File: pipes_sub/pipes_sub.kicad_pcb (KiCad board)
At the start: 4 copper layers, 70.8 x 110 mm, 272 parts, among them J1 2x8 Header, J2 2x5 Header, J4 2x5 Header, U1 CD4046, U10 CD4046, U11 CD4046, U12 CD4046, U13 CD4017, U14 CD4017, U15 CD4017, U16 CD4046, U17 CD4046, U18 CD4017, U19 CD4017, U2 TL072CP, U20 GLV5549, U21 GLV5549, U22 GLV5549, U23 TL072CP, U24 TL072CP, U25 TL072CP, U26 GLV5549, U27 GLV5549, U28 GLV5549, U29 TL072CP, U3 CD4017, U30 TL072CP, U31 TL072CP, U32 GLV5549, U33 GLV5549, U34 TL072CP, U35 TL072CP, U38 TL072CP, U39 TL072CP, U4 CD4046, U5 CD4046, U6 TL072CP, U7 CD4017, U8 CD4017, U9 TL072CP

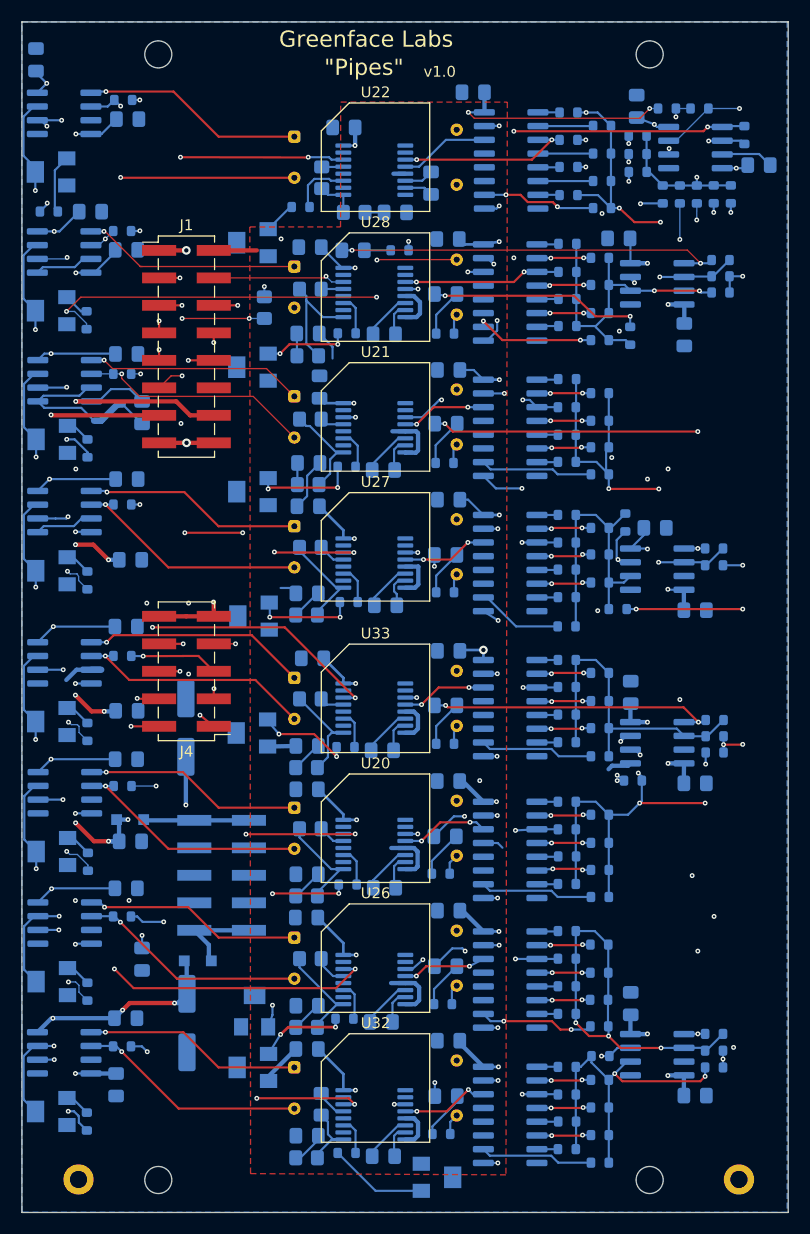
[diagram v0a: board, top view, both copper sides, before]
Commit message: Adds digikey bom merge. Uses local graphics for panel.
Adds bambooh graphics
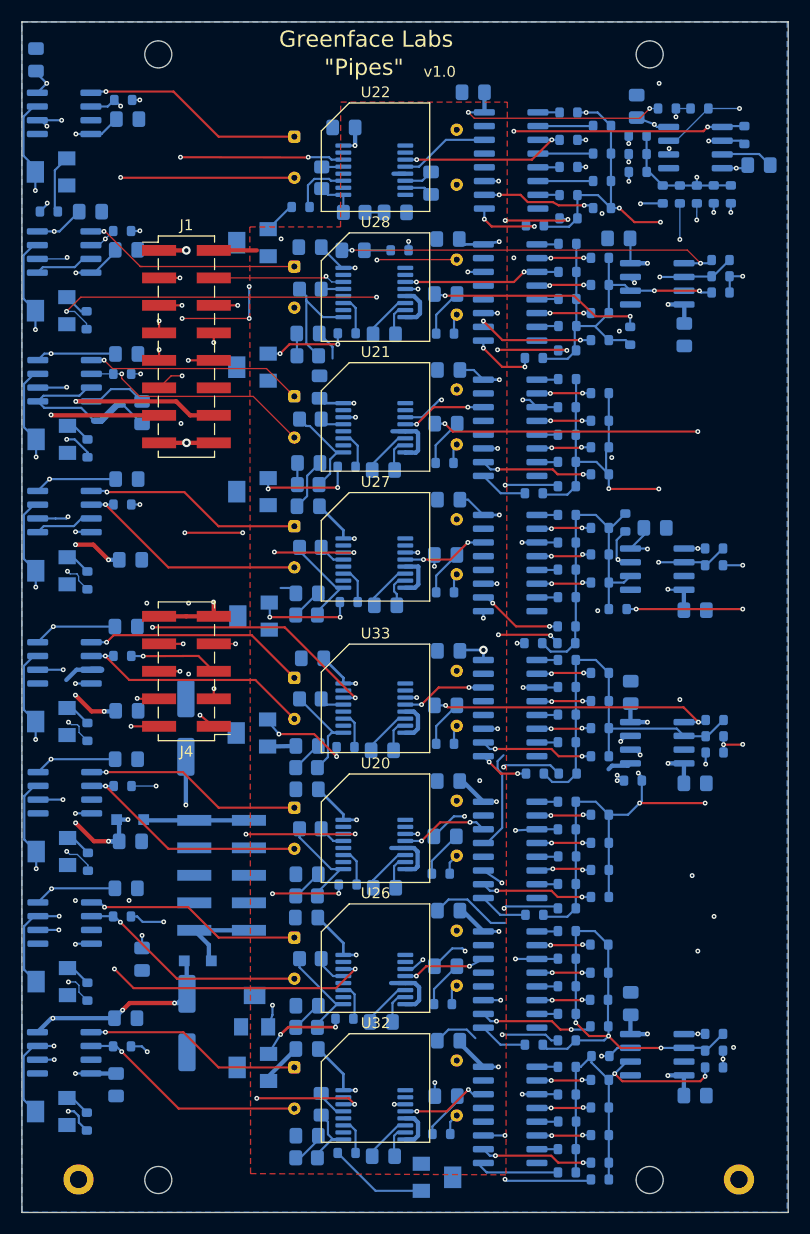
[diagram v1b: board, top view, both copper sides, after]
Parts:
- removed R2: 470, Resistor_SMD:R_0805_2012Metric_Pad1.20x1.40mm_HandSolder
- added R141: 300K, Resistor_SMD:R_0603_1608Metric, B.Cu at (87.4, 58.8)
- added R142: 300K, Resistor_SMD:R_0603_1608Metric, B.Cu at (87.3, 83.5)
- added R143: 249K, Resistor_SMD:R_0603_1608Metric, B.Cu at (90.5, 58.1)
- added R144: 249K, Resistor_SMD:R_0603_1608Metric, B.Cu at (90.3, 82.9)
- added R145: 300K, Resistor_SMD:R_0603_1608Metric, B.Cu at (87.3, 71.0)
- added R146: 300K, Resistor_SMD:R_0603_1608Metric, B.Cu at (87.2, 97.4)
- added R147: 249K, Resistor_SMD:R_0603_1608Metric, B.Cu at (90.4, 70.3)
- added R148: 249K, Resistor_SMD:R_0603_1608Metric, B.Cu at (90.3, 97.4)
- added R149: 300K, Resistor_SMD:R_0603_1608Metric, B.Cu at (87.4, 109.5)
- added R150: 300K, Resistor_SMD:R_0603_1608Metric, B.Cu at (87.3, 134.5)
- added R151: 249K, Resistor_SMD:R_0603_1608Metric, B.Cu at (90.4, 109.5)
- added R152: 249K, Resistor_SMD:R_0603_1608Metric, B.Cu at (90.3, 134.1)
- added R153: 300K, Resistor_SMD:R_0603_1608Metric, B.Cu at (90.3, 146.3)
- added R154: 300K, Resistor_SMD:R_0603_1608Metric, B.Cu at (87.3, 122.5)
- added R155: 249K, Resistor_SMD:R_0603_1608Metric, B.Cu at (93.4, 146.9)
- added R156: 249K, Resistor_SMD:R_0603_1608Metric, B.Cu at (90.3, 121.9)
- C1, C15, C21: value 4.7nF -> 300p
- C14, C22, C27, C28: value 1nF -> 300p
- C17, C18, C2, C23, C24, C25, C37, C38: value 1uF -> 10uF
- C20: value 2.2nF -> 300p
- R1, R10, R11, R12, R13, R139, R14, R140, R15, R16, R17: value 1K -> 10K
- R100, R104, R120, R124, R19, R7, R80, R84: value 300K -> 150K
- R101, R105, R121, R125, R22, R8, R81, R85: value 200K -> 165K
- R102, R106, R122, R126, R27, R82, R86, R9: value 150K -> 249K
- R107, R112, R127, R132, R28, R72, R87, R92: value 274K -> 165K
- R108, R113, R128, R133, R68, R73, R88, R93: value 274K -> 150K
- R109, R114, R129, R134, R69, R74, R89, R94: value 158K -> 200K
- R110, R115, R130, R135, R70, R75, R90, R95: value 158K -> 300K
- R20, R21, R29, R3, R30, R31, R38, R39: value 24.9K -> 10K
- R23, R25, R32, R34, R36, R4, R40, R42: value 200K -> 27K
- R24, R26, R33, R35, R37, R41, R43, R5: value 10K -> 1.5K
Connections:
- net VCO1 renamed SIG1
- net VCO2 renamed SIG2
- net VCO3 renamed SIG3
- net VCO4 renamed SIG4
- net VCO5 renamed SIG5
- net VCO6 renamed SIG6
- net VCO7 renamed SIG7
- net VCO8 renamed SIG8
- J1 pad 11: VCO -> SIG
- R1 pad 1: Net-(R1-Pad1) -> SIG
- U13 pad 11: unconnected-(U13-Pad11) -> Net-(R148-Pad1)
- U13 pad 15: Net-(U13-Pad15) -> GND
- U13 pad 9: Net-(U13-Pad15) -> Net-(R146-Pad1)
- U14 pad 11: unconnected-(U14-Pad11) -> Net-(R152-Pad1)
- U14 pad 15: Net-(U14-Pad15) -> GND
- U14 pad 9: Net-(U14-Pad15) -> Net-(R150-Pad1)
- U15 pad 11: unconnected-(U15-Pad11) -> Net-(R147-Pad1)
- U15 pad 15: Net-(U15-Pad15) -> GND
- U15 pad 9: Net-(U15-Pad15) -> Net-(R145-Pad1)
- U18 pad 11: unconnected-(U18-Pad11) -> Net-(R155-Pad1)
- U18 pad 15: Net-(U18-Pad15) -> GND
- U18 pad 9: Net-(U18-Pad15) -> Net-(R153-Pad1)
- U19 pad 11: unconnected-(U19-Pad11) -> Net-(R151-Pad1)
- U19 pad 15: Net-(U19-Pad15) -> GND
- U19 pad 9: Net-(U19-Pad15) -> Net-(R149-Pad1)
- U2 pad 1: Net-(R1-Pad1) -> SIG
- U3 pad 11: unconnected-(U3-Pad11) -> Net-(R143-Pad1)
- U3 pad 15: Net-(U3-Pad15) -> GND
- U3 pad 9: Net-(U3-Pad15) -> Net-(R141-Pad1)
- U7 pad 11: unconnected-(U7-Pad11) -> Net-(R156-Pad1)
- U7 pad 15: Net-(U7-Pad15) -> GND
- U7 pad 9: Net-(U7-Pad15) -> Net-(R154-Pad1)
- U8 pad 11: unconnected-(U8-Pad11) -> Net-(R144-Pad1)
- U8 pad 15: Net-(U8-Pad15) -> GND
- U8 pad 9: Net-(U8-Pad15) -> Net-(R142-Pad1)
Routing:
- net SIG: track 0.00 -> 75.8 mm, vias 0 -> 7
- net Net-(R1-Pad1): track 58.3 -> 0.00 mm, vias 4 -> 0
- net GND: track 103.7 -> 123.1 mm
- net VCO: track 15.5 -> 0.00 mm, vias 3 -> 0
- net Net-(U8-Pad15): track 15.4 -> 0.00 mm, vias 2 -> 0
- net Net-(R155-Pad1): track 0.00 -> 14.1 mm, vias 0 -> 2
- net Net-(R147-Pad1): track 0.00 -> 11.9 mm, vias 0 -> 3
- net Net-(R148-Pad1): track 0.00 -> 11.8 mm, vias 0 -> 3
- net Net-(R143-Pad1): track 0.00 -> 11.8 mm, vias 0 -> 3
- net Net-(U13-Pad15): track 11.4 -> 0.00 mm, vias 2 -> 0
- net Net-(R151-Pad1): track 0.00 -> 10.6 mm, vias 0 -> 2
- net Net-(U14-Pad15): track 10.5 -> 0.00 mm, vias 2 -> 0
- net Net-(U18-Pad15): track 10.3 -> 0.00 mm, vias 2 -> 0
- net Net-(U3-Pad15): track 10.3 -> 0.00 mm, vias 2 -> 0
- net Net-(U7-Pad15): track 10.2 -> 0.00 mm, vias 2 -> 0
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
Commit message: Version 1.1 of boards
Changes to use NSL-32SR3 Vactrols
Fixes 3904 package
Adds 10-step waveform
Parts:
- added C3: 30p, Capacitor_SMD:C_0805_2012Metric_Pad1.18x1.45mm_HandSolder, B.Cu at (104.5, 60.2)
- added C70: 30p, Capacitor_SMD:C_0805_2012Metric_Pad1.18x1.45mm_HandSolder, B.Cu at (103.9, 86.8)
- added C71: 30p, Capacitor_SMD:C_0805_2012Metric_Pad1.18x1.45mm_HandSolder, B.Cu at (98.2, 69.1)
- added C72: 30p, Capacitor_SMD:C_0805_2012Metric_Pad1.18x1.45mm_HandSolder, B.Cu at (98.5, 84.7)
- added C73: 30p, Capacitor_SMD:C_0805_2012Metric_Pad1.18x1.45mm_HandSolder, B.Cu at (104.0, 102.7)
- added C74: 30p, Capacitor_SMD:C_0805_2012Metric_Pad1.18x1.45mm_HandSolder, B.Cu at (103.9, 131.6)
- added C75: 30p, Capacitor_SMD:C_0805_2012Metric_Pad1.18x1.45mm_HandSolder, B.Cu at (97.2, 139.3)
- added C76: 30p, Capacitor_SMD:C_0805_2012Metric_Pad1.18x1.45mm_HandSolder, B.Cu at (93.7, 110.5)
- added R157: 200K, Resistor_SMD:R_0603_1608Metric, B.Cu at (58.3, 50.8)
- added R158: 200K, Resistor_SMD:R_0603_1608Metric, B.Cu at (52.4, 110.3)
- added R159: 200K, Resistor_SMD:R_0603_1608Metric, B.Cu at (48.7, 78.2)
- added R160: 200K, Resistor_SMD:R_0603_1608Metric, B.Cu at (49.5, 112.0)
- added R161: 200K, Resistor_SMD:R_0603_1608Metric, B.Cu at (51.1, 78.8)
- added R162: 200K, Resistor_SMD:R_0603_1608Metric, B.Cu at (49.2, 124.7)
- added R163: 200K, Resistor_SMD:R_0603_1608Metric, B.Cu at (50.6, 92.9)
- added R164: 200K, Resistor_SMD:R_0603_1608Metric, B.Cu at (50.1, 66.5)
- added R165: 200K, Resistor_SMD:R_0603_1608Metric, B.Cu at (52.5, 64.9)
- added R166: 200K, Resistor_SMD:R_0603_1608Metric, B.Cu at (50.1, 127.1)
- added R167: 200K, Resistor_SMD:R_0603_1608Metric, B.Cu at (52.4, 86.3)
- added R168: 200K, Resistor_SMD:R_0603_1608Metric, B.Cu at (49.2, 136.2)
- added R169: 200K, Resistor_SMD:R_0603_1608Metric, B.Cu at (56.9, 98.7)
- added R170: 200K, Resistor_SMD:R_0603_1608Metric, B.Cu at (49.9, 138.6)
- added R171: 200K, Resistor_SMD:R_0603_1608Metric, B.Cu at (52.9, 98.7)
- added R2: 200K, Resistor_SMD:R_0603_1608Metric, B.Cu at (55.9, 51.6)
- R100, R104, R120, R124, R19, R7, R80, R84: value 150K -> 154K
- R101, R105, R121, R125, R22, R8, R81, R85: value 165K -> 210K
- R102, R106, R122, R126, R27, R82, R86, R9: value 249K -> 300K
- R103, R119, R123, R18, R6, R79, R83, R99: value 200K -> 162K
- R107, R112, R127, R132, R28, R72, R87, R92: value 165K -> 150K
- R108, R113, R128, R133, R68, R73, R88, R93: value 150K -> 174K
- R109, R114, R129, R134, R69, R74, R89, R94: value 200K -> 261K
- R110, R115, R130, R135, R70, R75, R90, R95: value 300K -> 287K
- R141, R142, R145, R146, R149, R150, R153, R154: value 300K -> 237K
- R143, R144, R147, R148, R151, R152, R155, R156: value 249K -> 191K
- R45, R47, R49, R54, R56, R58, R63, R65: value 33K -> 220K
- R50, R51, R52, R59, R60, R61, R66, R67: value 24.9K -> 20K
- RV2, RV3, RV4, RV5, RV6, RV7, RV8, RV9: footprint sputterizer:Potentiometer_Bourns_3224W_Vertical -> Potentiometer_SMD:Potentiometer_Bourns_3224W_Vertical
- U20, U21, U22, U26, U27, U28, U32, U33: value GLV5549 -> NSL-32SR3
- moved C67 3.87 mm to (47.2, 127.0), turned to 180 degrees
- moved C57 2.09 mm to (49.6, 63.1)
- moved C69 1.74 mm to (47.1, 139.0), turned to 180 degrees
- moved C55 1.38 mm to (49.6, 50.4)
- moved R58 1.28 mm to (49.1, 60.6)
- moved R49 0.78 mm to (49.8, 47.9)
- moved R45 0.15 mm to (49.3, 110.5)
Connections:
- R45 pad 2: VCA6 -> GND
- R47 pad 2: VCA3 -> GND
- R49 pad 2: VCA1 -> GND
- R54 pad 2: VCA7 -> GND
- R56 pad 2: VCA4 -> GND
- R58 pad 2: VCA2 -> GND
- R63 pad 2: VCA8 -> GND
- R65 pad 2: VCA5 -> GND
- U20 pad 1: Net-(U20-Pad1) -> Net-(R45-Pad1)
- U20 pad 2: Net-(R45-Pad1) -> Net-(U20-Pad2)
- U21 pad 1: Net-(U21-Pad1) -> Net-(R47-Pad1)
- U21 pad 2: Net-(R47-Pad1) -> Net-(U21-Pad2)
- U22 pad 1: Net-(U22-Pad1) -> Net-(R49-Pad1)
- U22 pad 2: Net-(R49-Pad1) -> Net-(U22-Pad2)
- U23 pad 1: Net-(U20-Pad1) -> Net-(U20-Pad2)
- U23 pad 3: GND -> Net-(R158-Pad2)
- U24 pad 1: Net-(U21-Pad1) -> Net-(U21-Pad2)
- U24 pad 3: GND -> Net-(R159-Pad2)
- U25 pad 1: Net-(U22-Pad1) -> Net-(U22-Pad2)
- U25 pad 3: GND -> Net-(R157-Pad2)
- U26 pad 1: Net-(U26-Pad1) -> Net-(R54-Pad1)
- U26 pad 2: Net-(R54-Pad1) -> Net-(U26-Pad2)
- U27 pad 1: Net-(U27-Pad1) -> Net-(R56-Pad1)
- U27 pad 2: Net-(R56-Pad1) -> Net-(U27-Pad2)
- U28 pad 1: Net-(U28-Pad1) -> Net-(R58-Pad1)
- U28 pad 2: Net-(R58-Pad1) -> Net-(U28-Pad2)
- U29 pad 1: Net-(U26-Pad1) -> Net-(U26-Pad2)
- U29 pad 3: GND -> Net-(R162-Pad2)
- U30 pad 1: Net-(U27-Pad1) -> Net-(U27-Pad2)
- U30 pad 3: GND -> Net-(R163-Pad2)
- U31 pad 1: Net-(U28-Pad1) -> Net-(U28-Pad2)
- U31 pad 3: GND -> Net-(R164-Pad2)
- U32 pad 1: Net-(U32-Pad1) -> Net-(R63-Pad1)
- U32 pad 2: Net-(R63-Pad1) -> Net-(U32-Pad2)
- U33 pad 1: Net-(U33-Pad1) -> Net-(R65-Pad1)
- U33 pad 2: Net-(R65-Pad1) -> Net-(U33-Pad2)
- U34 pad 1: Net-(U32-Pad1) -> Net-(U32-Pad2)
- U34 pad 3: GND -> Net-(R168-Pad2)
- U35 pad 1: Net-(U33-Pad1) -> Net-(U33-Pad2)
- U35 pad 3: GND -> Net-(R169-Pad2)
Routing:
- net Net-(U28-Pad2): track 0.00 -> 27.9 mm, vias 0 -> 2
- net Net-(U22-Pad2): track 0.00 -> 26.6 mm, vias 0 -> 2
- net Net-(U33-Pad2): track 0.00 -> 26.2 mm, vias 0 -> 2
- net Net-(U32-Pad2): track 0.00 -> 25.9 mm, vias 0 -> 3
- net Net-(U27-Pad2): track 0.00 -> 25.8 mm, vias 0 -> 3
- net Net-(U20-Pad2): track 0.00 -> 25.1 mm, vias 0 -> 2
- net Net-(U21-Pad2): track 0.00 -> 24.9 mm, vias 0 -> 2
- net Net-(U26-Pad2): track 0.00 -> 24.8 mm, vias 0 -> 2
- net GND: track 123.1 -> 99.7 mm
- net Net-(U33-Pad1): track 20.7 -> 0.00 mm, vias 1 -> 0
- net Net-(U22-Pad1): track 20.6 -> 0.00 mm, vias 1 -> 0
- net Net-(U28-Pad1): track 20.3 -> 0.00 mm, vias 1 -> 0
- net Net-(U21-Pad1): track 20.1 -> 0.00 mm, vias 1 -> 0
- net Net-(U32-Pad1): track 20.1 -> 0.00 mm, vias 1 -> 0
- net Net-(U27-Pad1): track 20.1 -> 0.00 mm, vias 1 -> 0
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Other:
- board text added: "S/N 1.1."
- board text added: "v1.1"
- board text removed: "S/N 1.0."
- board text removed: "v1.0"

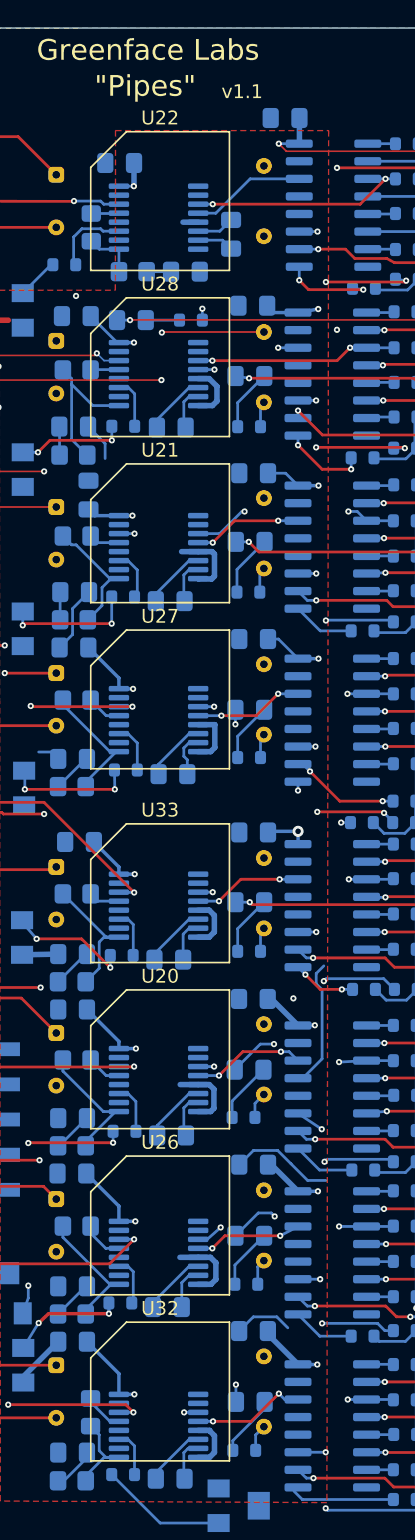
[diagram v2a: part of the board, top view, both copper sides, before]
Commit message: Uses new vactrols.
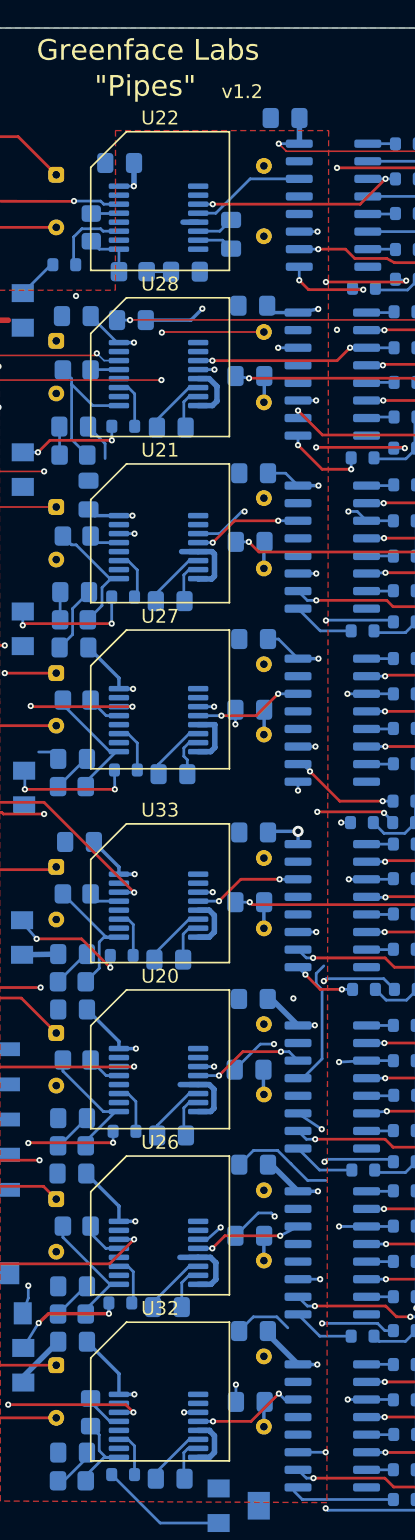
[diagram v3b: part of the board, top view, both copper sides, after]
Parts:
- removed R44, R46, R48, R53, R55, R57, R62, R64: 10K, Resistor_SMD:R_0603_1608Metric
- C46, C47, C48, C49, C50, C51, C52, C53: value 10uF -> 22uF
- R45, R47, R49, R54, R56, R58, R63, R65: value 220K -> 20K
- R50, R51, R52, R59, R60, R61, R66, R67: value 20K -> 430
- RV2, RV3, RV4, RV5, RV6, RV7, RV8, RV9: value 20K -> 500
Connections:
- C46 pad 2: Net-(C46-Pad2) -> Net-(U20-Pad4)
- C47 pad 2: Net-(C47-Pad2) -> Net-(U21-Pad4)
- C48 pad 2: Net-(C48-Pad2) -> Net-(U22-Pad4)
- C51 pad 2: Net-(C51-Pad2) -> Net-(U28-Pad4)
- C52 pad 2: Net-(C52-Pad2) -> Net-(U32-Pad4)
- U20 pad 4: Net-(R44-Pad2) -> Net-(U20-Pad4)
- U21 pad 4: Net-(R46-Pad2) -> Net-(U21-Pad4)
- U22 pad 4: Net-(R48-Pad2) -> Net-(U22-Pad4)
- U26 pad 4: Net-(R53-Pad2) -> Net-(C49-Pad2)
- U27 pad 4: Net-(R55-Pad2) -> Net-(C50-Pad2)
- U28 pad 4: Net-(R57-Pad2) -> Net-(U28-Pad4)
- U32 pad 4: Net-(R62-Pad2) -> Net-(U32-Pad4)
- U33 pad 4: Net-(R64-Pad2) -> Net-(C53-Pad2)
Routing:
- net Net-(U22-Pad4): track 0.00 -> 11.5 mm, vias 0 -> 1
- net Net-(R48-Pad2): track 7.90 -> 0.00 mm, vias 1 -> 0
- net Net-(C51-Pad2): track 4.46 -> 0.00 mm
- net Net-(C47-Pad2): track 4.46 -> 0.00 mm
- net Net-(C52-Pad2): track 4.45 -> 0.00 mm
- net Net-(C46-Pad2): track 4.39 -> 0.00 mm
- net Net-(C49-Pad2): track 4.38 -> 1.80 mm
- net Net-(C50-Pad2): track 4.24 -> 1.80 mm
- net Net-(C53-Pad2): track 4.34 -> 1.90 mm
- net Net-(C48-Pad2): track 2.44 -> 0.00 mm
- net Net-(R62-Pad2): track 1.96 -> 0.00 mm
- net Net-(U21-Pad4): track 0.00 -> 1.94 mm
- net Net-(R44-Pad2): track 1.93 -> 0.00 mm
- net Net-(U28-Pad4): track 0.00 -> 1.91 mm
- net Net-(R53-Pad2): track 1.89 -> 0.00 mm
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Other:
- board text added: "S/N 1.2."
- board text added: "v1.2"
- board text removed: "S/N 1.1."
- board text removed: "v1.1"
